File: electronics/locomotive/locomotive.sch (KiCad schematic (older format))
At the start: 9 parts

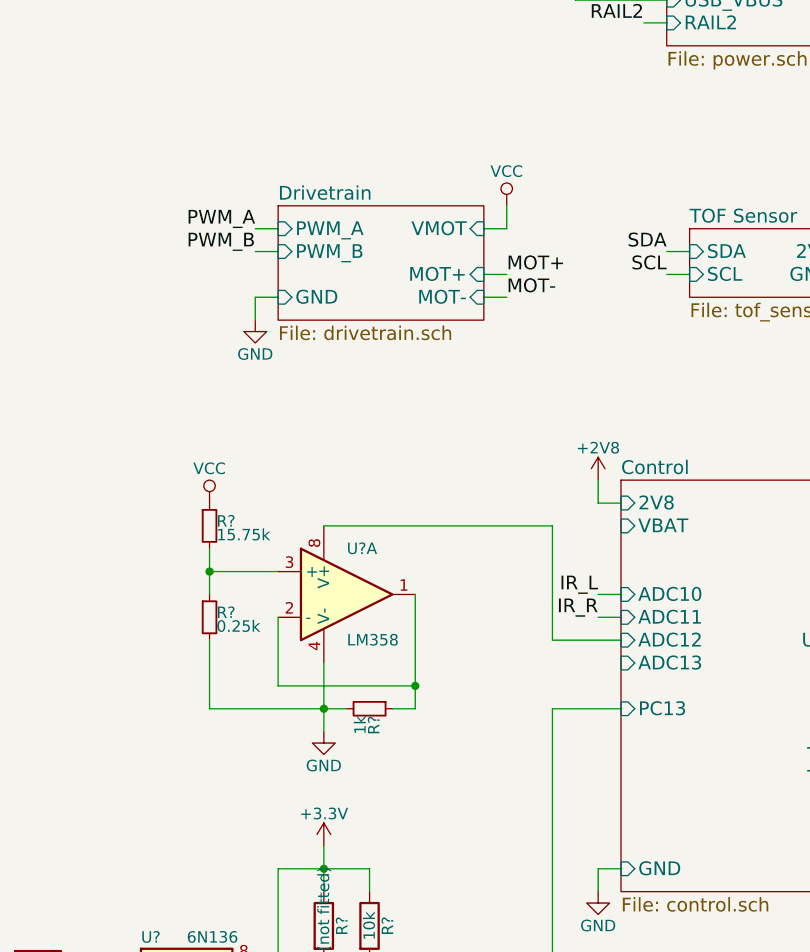
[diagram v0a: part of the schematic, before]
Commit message: electronics: locomotive: Update schematics
Voltage regulator, TOF, IR receiver, voltage scaler, I2C control lines, power
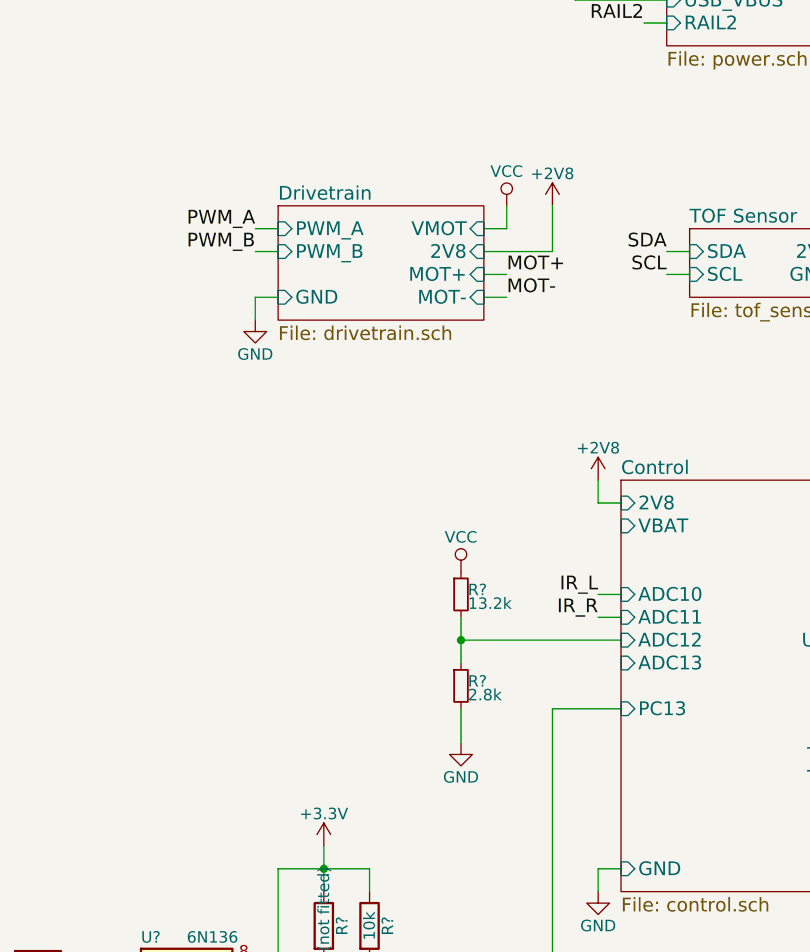
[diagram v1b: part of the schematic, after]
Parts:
- removed R?: 1k, symbol R_Small
- removed U?: LM358, symbol LM358
- R?: value 0.25k -> 2.8k
- R?: value 15.75k -> 13.2k
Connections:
- net Control/ADC12: now also R?.1, R?.2
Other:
- moved on the sheet: R?
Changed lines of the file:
@@
 LIBS:valves
 LIBS:stm32
+LIBS:SPX3819
 LIBS:bcan
+LIBS:TSOP57238
 LIBS:locomotive-cache
 EELAYER 25 0
@@
 $EndSheet
 $Comp
-L +2V8 #PWR?
+L +2V8 #PWR01
 U 1 1 58B1F309
 P 4900 4300
-F 0 "#PWR?" H 4900 4150 50  0001 C CNN
+F 0 "#PWR01" H 4900 4150 50  0001 C CNN
 F 1 "+2V8" H 4900 4440 50  0000 C CNN
 F 2 "" H 4900 4300 50  0001 C CNN
@@
 $EndComp
 $Comp
-L +2V8 #PWR?
+L +2V8 #PWR02
 U 1 1 58B1F498
 P 6300 2000
-F 0 "#PWR?" H 6300 1850 50  0001 C CNN
+F 0 "#PWR02" H 6300 1850 50  0001 C CNN
 F 1 "+2V8" H 6300 2140 50  0000 C CNN
 F 2 "" H 6300 2000 50  0001 C CNN
@@
 $EndComp
 $Comp
-L GND #PWR?
+L GND #PWR03
 U 1 1 58B1F533
 P 6300 2400
-F 0 "#PWR?" H 6300 2150 50  0001 C CNN
+F 0 "#PWR03" H 6300 2150 50  0001 C CNN
 F 1 "GND" H 6300 2250 50  0000 C CNN
 F 2 "" H 6300 2400 50  0000 C CNN
@@
 $EndComp
 $Comp
-L GND #PWR?
+L GND #PWR04
 U 1 1 58B1F5CE
 P 4900 6100
-F 0 "#PWR?" H 4900 5850 50  0001 C CNN
+F 0 "#PWR04" H 4900 5850 50  0001 C CNN
 F 1 "GND" H 4900 5950 50  0000 C CNN
 F 2 "" H 4900 6100 50  0000 C CNN
@@
 RAIL2
 $Comp
-L VCC #PWR?
+L VCC #PWR05
 U 1 1 58B20676
 P 6500 2000
-F 0 "#PWR?" H 6500 1850 50  0001 C CNN
+F 0 "#PWR05" H 6500 1850 50  0001 C CNN
 F 1 "VCC" H 6500 2150 50  0000 C CNN
 F 2 "" H 6500 2000 50  0001 C CNN
@@
 F6 "VMOT" I R 4400 3200 60
 F7 "GND" I L 3500 3500 60
+F8 "2V8" I R 4400 3300 60
 $EndSheet
 Text Label 4500 3400 0    60   ~ 0
@@
 PWM_B
 $Comp
-L VCC #PWR?
+L VCC #PWR06
 U 1 1 58B2A2C4
 P 4500 3100
-F 0 "#PWR?" H 4500 2950 50  0001 C CNN
+F 0 "#PWR06" H 4500 2950 50  0001 C CNN
 F 1 "VCC" H 4500 3250 50  0000 C CNN
 F 2 "" H 4500 3100 50  0001 C CNN
@@
 $EndComp
 $Comp
-L GND #PWR?
+L GND #PWR07
 U 1 1 58B2A383
 P 3400 3600
-F 0 "#PWR?" H 3400 3350 50  0001 C CNN
+F 0 "#PWR07" H 3400 3350 50  0001 C CNN
 F 1 "GND" H 3400 3450 50  0000 C CNN
 F 2 "" H 3400 3600 50  0000 C CNN
@@
 $EndComp
 $Comp
-L LM358 U?
-U 1 1 58B2BF2A
-P 3800 4800
-F 0 "U?" H 3800 5000 50  0000 L CNN
-F 1 "LM358" H 3800 4600 50  0000 L CNN
-F 2 "" H 3800 4800 50  0001 C CNN
-F 3 "" H 3800 4800 50  0001 C CNN
-	1    3800 4800
-	1    0    0    -1
-$EndComp
-$Comp
 L R_Small R?
 U 1 1 58B2C8A8
-P 3200 4900
-F 0 "R?" H 3230 4920 50  0000 L CNN
-F 1 "0.25k" H 3230 4860 50  0000 L CNN
-F 2 "" H 3200 4900 50  0001 C CNN
-F 3 "" H 3200 4900 50  0001 C CNN
-	1    3200 4900
+P 4300 5200
+F 0 "R?" H 4330 5220 50  0000 L CNN
+F 1 "2.8k" H 4330 5160 50  0000 L CNN
+F 2 "" H 4300 5200 50  0001 C CNN
+F 3 "" H 4300 5200 50  0001 C CNN
+	1    4300 5200
 	1    0    0    -1
 $EndComp
@@
 L R_Small R?
 U 1 1 58B2CCB4
-P 3200 4500
-F 0 "R?" H 3230 4520 50  0000 L CNN
-F 1 "15.75k" H 3230 4460 50  0000 L CNN
-F 2 "" H 3200 4500 50  0001 C CNN
-F 3 "" H 3200 4500 50  0001 C CNN
-	1    3200 4500
-	1    0    0    -1
-$EndComp
-$Comp
-L GND #PWR?
-U 1 1 58B2D696
-P 3700 5400
-F 0 "#PWR?" H 3700 5150 50  0001 C CNN
-F 1 "GND" H 3700 5250 50  0000 C CNN
-F 2 "" H 3700 5400 50  0000 C CNN
-F 3 "" H 3700 5400 50  0000 C CNN
-	1    3700 5400
-	1    0    0    -1
-$EndComp
-$Comp
-L R_Small R?
-U 1 1 58B2E38E
-P 3900 5300
-F 0 "R?" H 3930 5320 50  0000 L CNN
-F 1 "1k" H 3930 5260 50  0000 L CNN
-F 2 "" H 3900 5300 50  0001 C CNN
-F 3 "" H 3900 5300 50  0001 C CNN
-	1    3900 5300
-	0    1    1    0
-$EndComp
-$Comp
-L VCC #PWR?
+P 4300 4800
+F 0 "R?" H 4330 4820 50  0000 L CNN
+F 1 "13.2k" H 4330 4760 50  0000 L CNN
+F 2 "" H 4300 4800 50  0001 C CNN
+F 3 "" H 4300 4800 50  0001 C CNN
+	1    4300 4800
+	1    0    0    -1
+$EndComp
+$Comp
+L VCC #PWR09
 U 1 1 58B2F261
-P 3200 4400
-F 0 "#PWR?" H 3200 4250 50  0001 C CNN
-F 1 "VCC" H 3200 4550 50  0000 C CNN
-F 2 "" H 3200 4400 50  0001 C CNN
-F 3 "" H 3200 4400 50  0001 C CNN
-	1    3200 4400
+P 4300 4700
+F 0 "#PWR09" H 4300 4550 50  0001 C CNN
+F 1 "VCC" H 4300 4850 50  0000 C CNN
+F 2 "" H 4300 4700 50  0001 C CNN
+F 3 "" H 4300 4700 50  0001 C CNN
+	1    4300 4700
 	1    0    0    -1
 $EndComp
@@
 $EndSheet
 $Comp
-L +5V #PWR?
+L +5V #PWR010
 U 1 1 58B31950
 P 4800 2000
-F 0 "#PWR?" H 4800 1850 50  0001 C CNN
+F 0 "#PWR010" H 4800 1850 50  0001 C CNN
 F 1 "+5V" H 4800 2140 50  0000 C CNN
 F 2 "" H 4800 2000 50  0001 C CNN
@@
 $EndComp
 $Comp
-L +5V #PWR?
+L +5V #PWR011
 U 1 1 58B31D04
 P 6400 4900
-F 0 "#PWR?" H 6400 4750 50  0001 C CNN
+F 0 "#PWR011" H 6400 4750 50  0001 C CNN
 F 1 "+5V" H 6400 5040 50  0000 C CNN
 F 2 "" H 6400 4900 50  0001 C CNN
@@
 SCL
 $Comp
-L +2V8 #PWR?
+L +2V8 #PWR012
 U 1 1 58B34E5C
 P 6300 3200
-F 0 "#PWR?" H 6300 3050 50  0001 C CNN
+F 0 "#PWR012" H 6300 3050 50  0001 C CNN
 F 1 "+2V8" H 6300 3340 50  0000 C CNN
 F 2 "" H 6300 3200 50  0001 C CNN
@@
 $EndComp
 $Comp
-L GND #PWR?
+L GND #PWR013
 U 1 1 58B35272
 P 6300 3500
-F 0 "#PWR?" H 6300 3250 50  0001 C CNN
+F 0 "#PWR013" H 6300 3250 50  0001 C CNN
 F 1 "GND" H 6300 3350 50  0000 C CNN
 F 2 "" H 6300 3500 50  0000 C CNN
@@
 SCL
 $Comp
-L GND #PWR?
+L GND #PWR014
 U 1 1 58B37782
 P 8000 3500
-F 0 "#PWR?" H 8000 3250 50  0001 C CNN
+F 0 "#PWR014" H 8000 3250 50  0001 C CNN
 F 1 "GND" H 8000 3350 50  0000 C CNN
 F 2 "" H 8000 3500 50  0000 C CNN
@@
 $EndComp
 $Comp
-L +2V8 #PWR?
+L +2V8 #PWR015
 U 1 1 58B37883
 P 8000 3200
-F 0 "#PWR?" H 8000 3050 50  0001 C CNN
+F 0 "#PWR015" H 8000 3050 50  0001 C CNN
 F 1 "+2V8" H 8000 3340 50  0000 C CNN
 F 2 "" H 8000 3200 50  0001 C CNN
@@
 	3400 3500 3400 3600
 Wire Wire Line
-	4100 5200 3500 5200
-Wire Wire Line
-	3500 5200 3500 4900
-Wire Wire Line
-	4100 4800 4100 5200
-Wire Wire Line
-	4100 5200 4100 5300
-Wire Wire Line
-	3700 5100 3700 5300
-Wire Wire Line
-	3700 5300 3700 5400
-Wire Wire Line
-	3200 5000 3200 5300
-Wire Wire Line
-	3200 5300 3700 5300
-Wire Wire Line
-	3700 5300 3800 5300
-Connection ~ 3700 5300
-Wire Wire Line
-	3500 4700 3200 4700
-Wire Wire Line
-	3200 4600 3200 4700
-Wire Wire Line
-	3200 4700 3200 4800
-Connection ~ 3200 4700
-Wire Wire Line
-	4100 5300 4000 5300
-Connection ~ 4100 5200
+	4300 5300 4300 5450
+Wire Wire Line
+	4300 4900 4300 5000
+Wire Wire Line
+	4300 5000 4300 5100
+Connection ~ 4300 5000
 Wire Wire Line
 	5200 2200 4800 2200
@@
 	6300 5300 6400 5300
 Wire Wire Line
-	3700 4500 4700 4500
-Wire Wire Line
-	4700 4500 4700 5000
-Wire Wire Line
-	4700 5000 5000 5000
+	4300 5000 5000 5000
 Wire Wire Line
 	4700 5300 5000 5300
@@
 	2700 6750 2700 6800
 Wire Wire Line
+	2200 6800 2700 6800
+Wire Wire Line
 	2700 6800 2800 6800
-Wire Wire Line
-	2200 6800 2700 6800
 Wire Wire Line
 	2800 6800 2800 6700
@@
 	2700 6450 2700 6400
 Wire Wire Line
+	2600 6400 2700 6400
+Wire Wire Line
 	2700 6400 2800 6400
-Wire Wire Line
-	2600 6400 2700 6400
 Wire Wire Line
 	2800 6400 2800 6500
@@
 	3500 6000 3500 6400
 Wire Wire Line
+	3700 5900 3700 6000
+Wire Wire Line
 	3700 6000 3700 6100
 Wire Wire Line
-	3700 5900 3700 6000
+	3500 6000 3700 6000
 Wire Wire Line
 	3700 6000 3900 6000
 Wire Wire Line
-	3500 6000 3700 6000
-Wire Wire Line
 	3900 6000 3900 6100
 Wire Wire Line
 	3900 6700 3900 6400
 Wire Wire Line
+	3400 6700 3900 6700
+Wire Wire Line
 	3900 6700 4700 6700
-Wire Wire Line
-	3400 6700 3900 6700
 Wire Wire Line
 	3500 6800 3500 6900
@@
 $EndComp
 $Comp
-L GND #PWR02
+L GND #PWR016
 U 1 1 58ACE876
 P 3500 6900
-F 0 "#PWR02" H 3500 6650 50  0001 C CNN
+F 0 "#PWR016" H 3500 6650 50  0001 C CNN
 F 1 "GND" H 3500 6750 50  0000 C CNN
 F 2 "" H 3500 6900 50  0000 C CNN
@@
 $EndComp
 $Comp
-L +3.3V #PWR01
+L +3.3V #PWR017
 U 1 1 58940D69
 P 3700 5900
-F 0 "#PWR01" H 3700 5750 50  0001 C CNN
+F 0 "#PWR017" H 3700 5750 50  0001 C CNN
 F 1 "+3.3V" H 3700 6040 50  0000 C CNN
 F 2 "" H 3700 5900 50  0000 C CNN
@@
 	0    1    1    0
 $EndComp
+$Comp
+L +2V8 #PWR018
+U 1 1 58C4B58F
+P 4700 3100
+F 0 "#PWR018" H 4700 2950 50  0001 C CNN
+F 1 "+2V8" H 4700 3240 50  0000 C CNN
+F 2 "" H 4700 3100 50  0001 C CNN
+F 3 "" H 4700 3100 50  0001 C CNN
+	1    4700 3100
+	1    0    0    -1
+$EndComp
+Wire Wire Line
+	4400 3300 4700 3300
+Wire Wire Line
+	4700 3300 4700 3100
+$Comp
+L GND #PWR?
+U 1 1 58C6988A
+P 4300 5450
+F 0 "#PWR?" H 4300 5200 50  0001 C CNN
+F 1 "GND" H 4300 5300 50  0000 C CNN
+F 2 "" H 4300 5450 50  0000 C CNN
+F 3 "" H 4300 5450 50  0000 C CNN
+	1    4300 5450
+	1    0    0    -1
+$EndComp
 $EndSCHEMATC

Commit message: firmware: locomotive: Change voltage regulator resistor values
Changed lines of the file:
@@
 	4300 5300 4300 5450
 Wire Wire Line
-	4300 4900 4300 5000
-Wire Wire Line
-	4300 5000 4300 5100
+	4300 4900 4300 5100
 Connection ~ 4300 5000
 Wire Wire Line
@@
 	2700 6750 2700 6800
 Wire Wire Line
-	2200 6800 2700 6800
-Wire Wire Line
-	2700 6800 2800 6800
+	2200 6800 2800 6800
 Wire Wire Line
 	2800 6800 2800 6700
@@
 	2700 6450 2700 6400
 Wire Wire Line
-	2600 6400 2700 6400
-Wire Wire Line
-	2700 6400 2800 6400
+	2600 6400 2800 6400
 Wire Wire Line
 	2800 6400 2800 6500
@@
 	3500 6000 3500 6400
 Wire Wire Line
-	3700 5900 3700 6000
+	3700 5900 3700 6100
 Wire Wire Line
-	3700 6000 3700 6100
-Wire Wire Line
-	3500 6000 3700 6000
-Wire Wire Line
-	3700 6000 3900 6000
+	3500 6000 3900 6000
 Wire Wire Line
 	3900 6000 3900 6100
@@
 	3900 6700 3900 6400
 Wire Wire Line
-	3400 6700 3900 6700
-Wire Wire Line
-	3900 6700 4700 6700
+	3400 6700 4700 6700
 Wire Wire Line
 	3500 6800 3500 6900

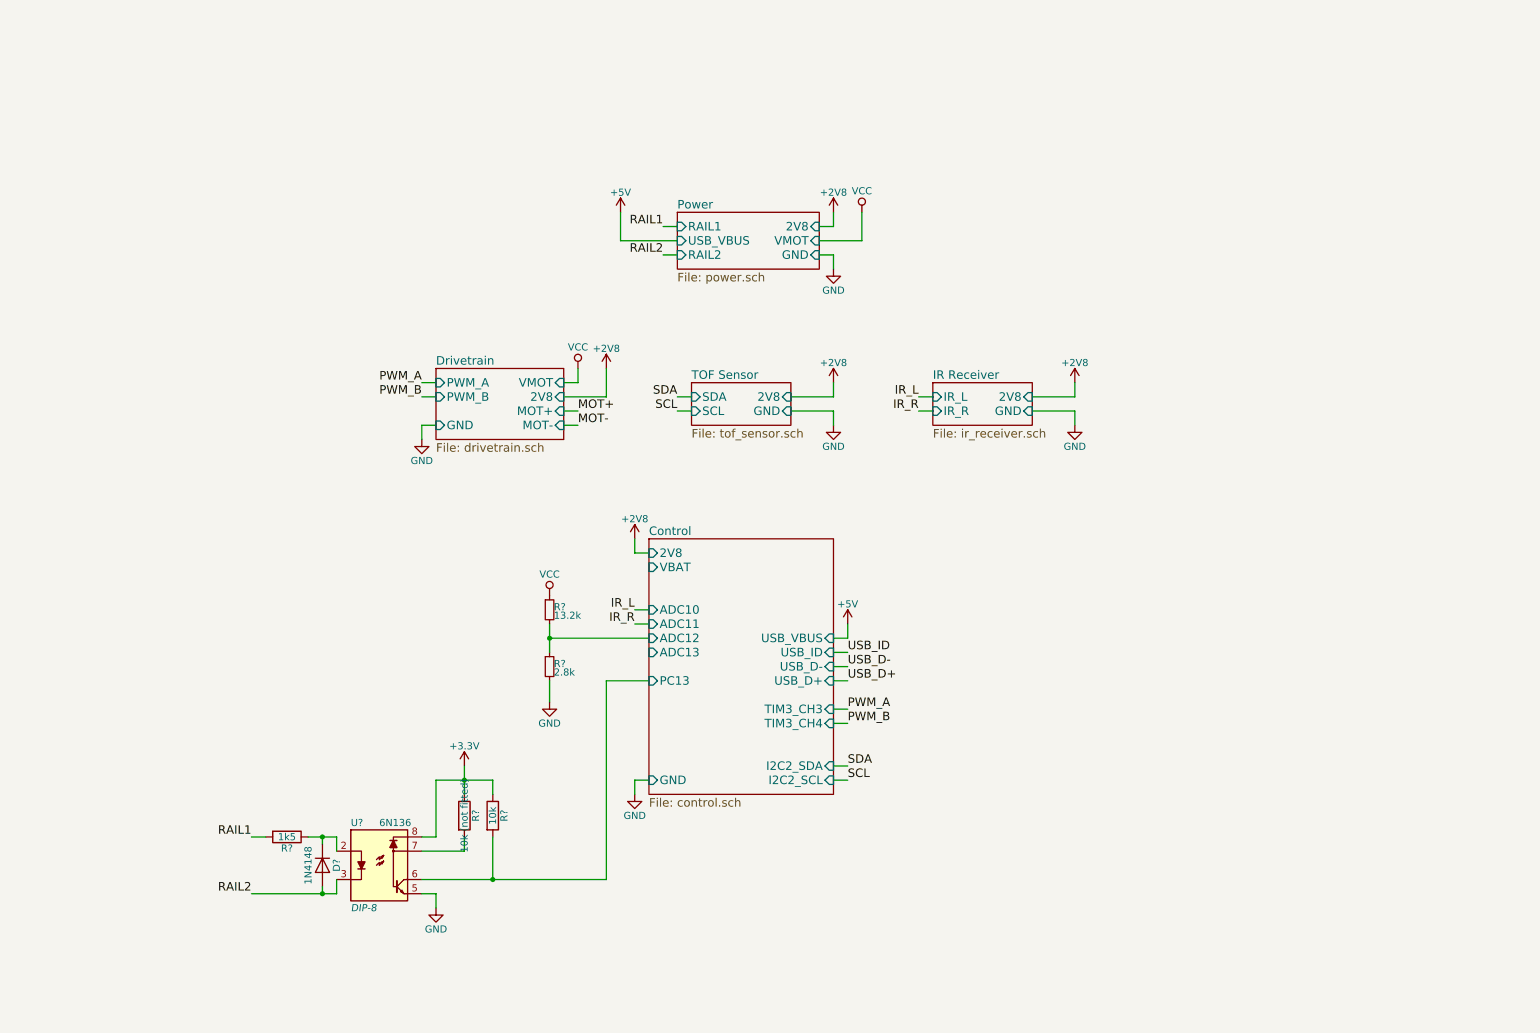
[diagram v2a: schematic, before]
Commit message: electronics: locomotive: Fix up schematics
- add all parts and label them
- some values still tentative
- still need to finish connectors
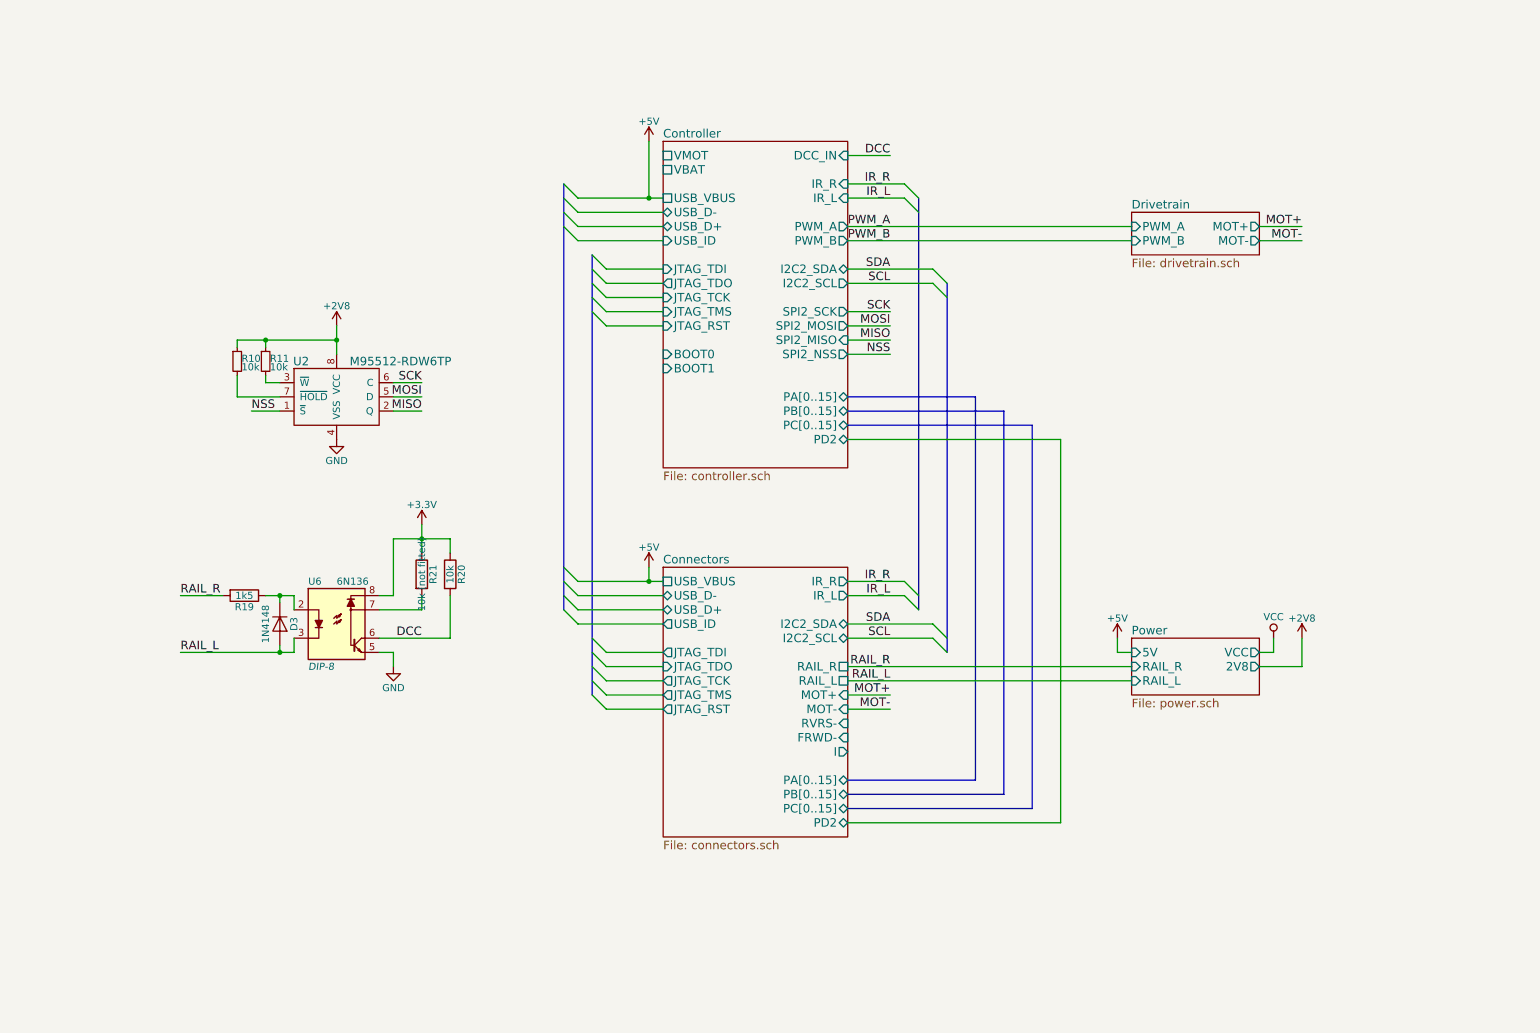
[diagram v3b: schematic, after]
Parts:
- removed R?: 2.8k, symbol R_Small
- removed R?: 13.2k, symbol R_Small
- added R10, R11: 10k, symbol R_Small
- added U2: M95512-RDW6TP, symbol M95512-RDW6TP
- gave numbers to parts that had none: 5
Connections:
- net +2V8: now also R10.1, R11.1, U2.8 (VCC)
- net GND: now also U2.4 (VSS)
- net Control/PC13 renamed DCC
- net RAIL1 renamed RAIL_R
- net RAIL2 renamed RAIL_L
- new net: R11.2, U2.3 (~W)
- new net: R10.2, U2.7 (~HOLD)
- new net MISO: U2.2 (Q)
- new net MOSI: U2.5 (D)
- new net NSS: U2.1 (~S)
- new net SCK: U2.6 (C)
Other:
- moved on the sheet: D3, R19, R20, R21, U6
